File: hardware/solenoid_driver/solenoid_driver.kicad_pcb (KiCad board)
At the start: 2 copper layers, 45.5 x 48.5 mm, 16 parts, among them J1 from_mainboard, J2 12V power, J3 to_solenoid2, J4 to_solenoid1, Q1 Q_NMOS_GDS, Q2 Q_NMOS_GDS

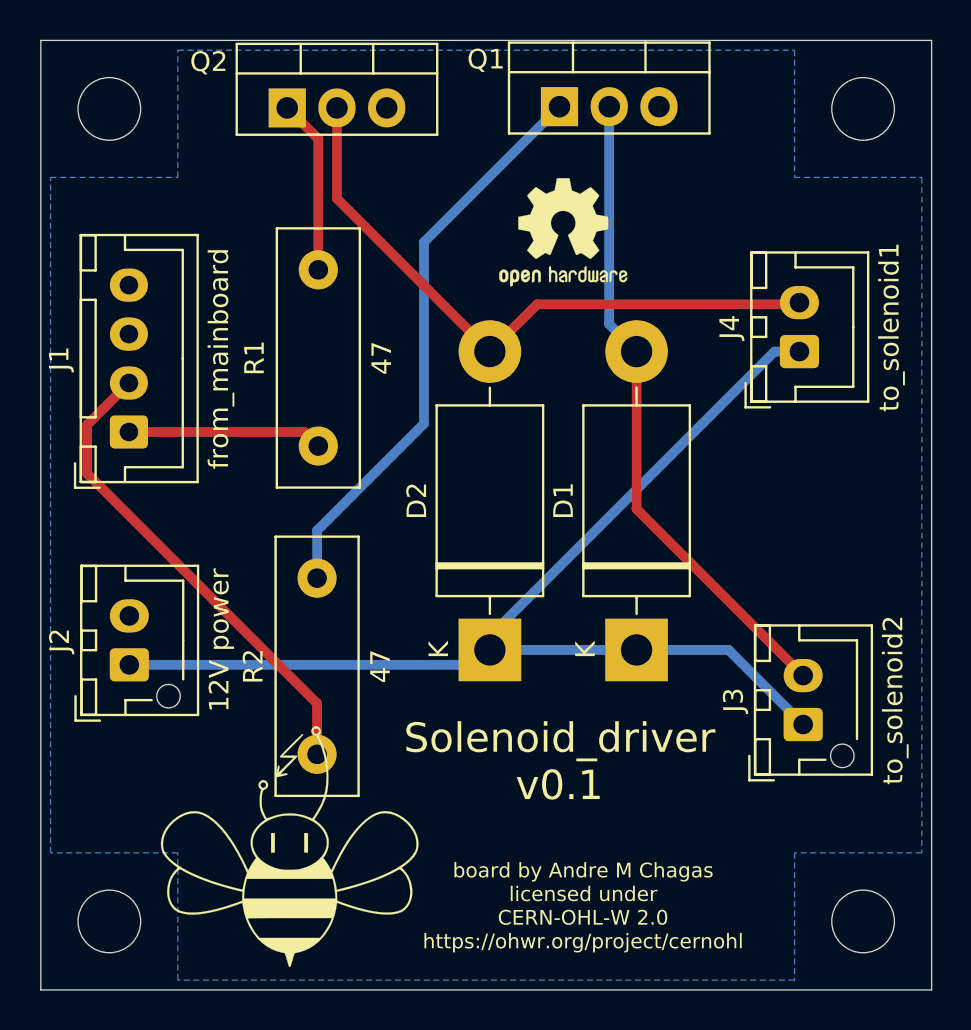
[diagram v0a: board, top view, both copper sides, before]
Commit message: cleanup of piezo amplifier and solenoid driver
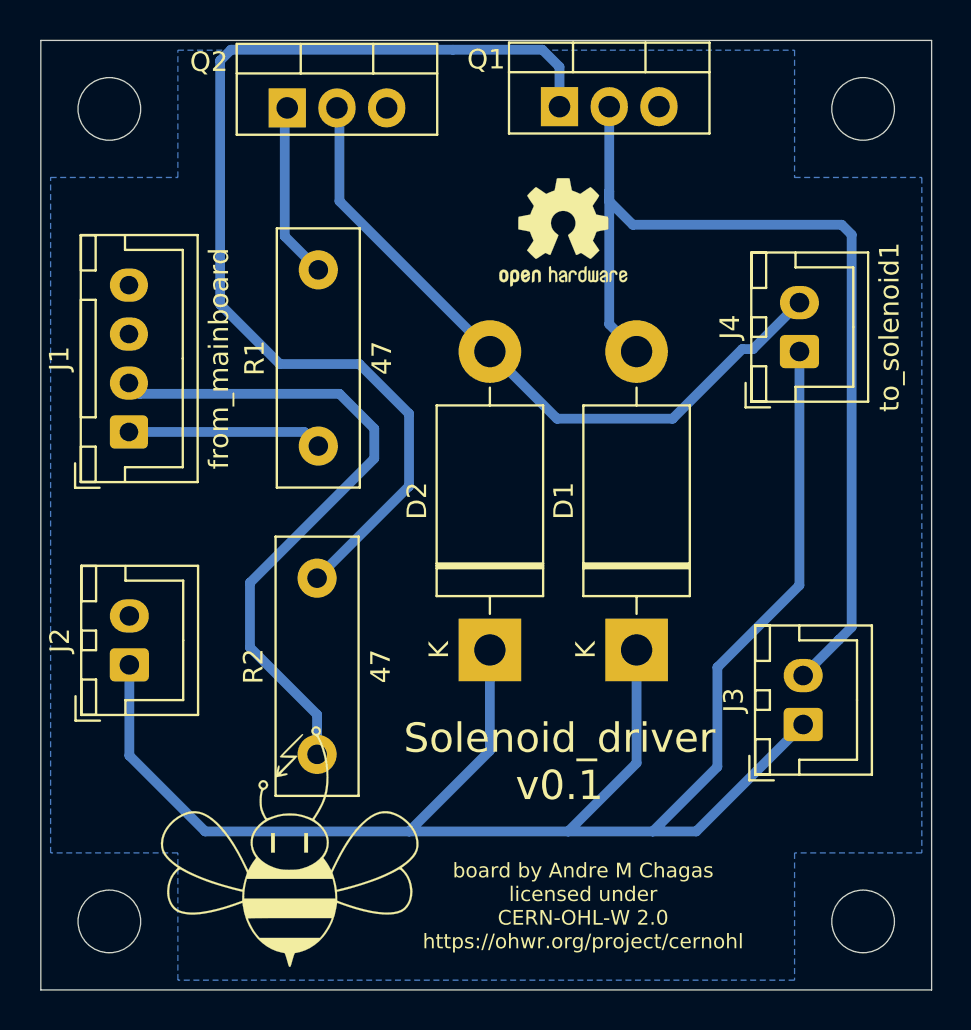
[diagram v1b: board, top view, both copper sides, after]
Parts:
- J2, J3: footprint Connector_JST:JST_XH_B2B-XH-AM_1x02_P2.50mm_Vertical -> Connector_JST:JST_XH_B2B-XH-A_1x02_P2.50mm_Vertical
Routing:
- net +12V: track 58.8 -> 92.2 mm
- net Net-(Q1-Pad1): track 29.2 -> 54.7 mm
- net Net-(D1-Pad2): track 33.2 -> 50.2 mm
- net solenoid2: track 24.7 -> 34.2 mm
- net Net-(D2-Pad2): track 32.5 -> 35.4 mm
